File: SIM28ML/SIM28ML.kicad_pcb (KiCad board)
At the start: 2 copper layers, 22.7 x 20.3 mm, 26 parts, among them J1 Conn_01x05, J2 Conn_01x05, U2 AP7365-W-7

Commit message: GNSS Boards Page Layout Updates
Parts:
- renumbered SIM28M to SIM28ML
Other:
- board text added: "SIM28ML www.SirBoard.com"
- board text removed: "SIM28M www.SirBoard.com"
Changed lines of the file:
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@@
     (thickness 1.6)
     (drawings 26)
-    (tracks 116)
+    (tracks 117)
     (zones 0)
     (modules 26)
@@
   (page User 132.004 102.006)
   (title_block
-    (title "SIM28M Based GPS Module")
+    (title "SIM28ML Based GPS Module")
     (date 2019-10-30)
     (rev 1)
     (company SirBoard)
-    (comment 1 "SIM28M is based on the MT3339 Chipset")
+    (comment 1 "SIM28ML is based on the MT3339 Chipset")
     (comment 2 "Breadboard Friendly Micro GPS Module")
   )
@@
     (tags "Integrated Circuit")
     (attr smd)
-    (fp_text reference SIM28M (at 4.85 5.05 90) (layer F.SilkS)
+    (fp_text reference SIM28ML (at 4.85 5.05 90) (layer F.SilkS)
       (effects (font (size 1.27 1.27) (thickness 0.254)))
     )
@@
     )
   )
-  (gr_text "SIM28M\nwww.SirBoard.com" (at 63.5 31.242 180) (layer B.SilkS)
+  (gr_text "SIM28ML\nwww.SirBoard.com" (at 63.5 31.242 180) (layer B.SilkS)
     (effects (font (size 1 0.9) (thickness 0.15)) (justify mirror))
   )
@@
   (segment (start 58.3565 44.454419) (end 58.3565 45.6565) (width 0.6) (layer B.Cu) (net 23))
   (segment (start 58.3565 41.8365) (end 58.3565 44.454419) (width 0.6) (layer B.Cu) (net 23))
-  (segment (start 68.272 35.6235) (end 68.2625 35.633) (width 0.25) (layer F.Cu) (net 23))
-  (segment (start 69.596 35.6235) (end 68.272 35.6235) (width 0.25) (layer F.Cu) (net 23))
-  (segment (start 71.501 36.0045) (end 69.977 36.0045) (width 0.25) (layer F.Cu) (net 23))
-  (segment (start 69.977 36.0045) (end 69.596 35.6235) (width 0.25) (layer F.Cu) (net 23))
   (segment (start 58.3565 37.465) (end 58.3565 41.8365) (width 0.6) (layer B.Cu) (net 23))
   (segment (start 55.5365 36.7665) (end 57.658 36.7665) (width 0.6) (layer B.Cu) (net 23))
@@
   (segment (start 58.3565 41.8365) (end 66.812 41.8365) (width 0.6) (layer B.Cu) (net 23))
   (segment (start 66.812 41.8365) (end 68.326 40.3225) (width 0.6) (layer B.Cu) (net 23))
+  (segment (start 68.272 35.6235) (end 68.2625 35.633) (width 0.25) (layer F.Cu) (net 23))
+  (segment (start 69.596 35.6235) (end 68.272 35.6235) (width 0.25) (layer F.Cu) (net 23))
+  (segment (start 70.104 36.1315) (end 69.596 35.6235) (width 0.25) (layer F.Cu) (net 23))
+  (segment (start 71.501 36.0045) (end 71.374 36.1315) (width 0.25) (layer F.Cu) (net 23))
+  (segment (start 71.374 36.1315) (end 70.104 36.1315) (width 0.25) (layer F.Cu) (net 23))
   (segment (start 53.1495 37.3) (end 53.1875 37.338) (width 0.25) (layer F.Cu) (net 24))
   (via (at 52.6415 38.2905) (size 0.6) (drill 0.3) (layers F.Cu B.Cu) (net 24))

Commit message: Power LED added
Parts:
- removed R7: 68K, Resistor_SMD:R_0603_1608Metric
- removed R8: 22K, Resistor_SMD:R_0603_1608Metric
- removed U2: AP7365-W-7, Package_TO_SOT_SMD:SOT-23-5
- added 3V: LED, LED_SMD:LED_0603_1608Metric, F.Cu at (73.9, 39.0)
- added LED: SolderJumper_2_Bridged, Jumper:SolderJumper-2_P1.3mm_Bridged_RoundedPad1.0x1.5mm, B.Cu at (73.2, 33.3)
- added R6: 680E, Resistor_SMD:R_0603_1608Metric, F.Cu at (73.9, 36.1)
- added U1: AP2127K-3.3, Package_TO_SOT_SMD:SOT-23-5, F.Cu at (71.5, 36.1)
- moved ANT 0.95 mm to (53.8, 40.5)
- renumbered JP1 to ANT, CR1220 to BT1, SIM28ML to IC1
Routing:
- net Net-(R7-Pad2): track 2.96 -> 0.00 mm
- net EN: track 15.7 -> 13.3 mm
- net Net-(JP2-Pad2): track 0.00 -> 2.05 mm, vias 0 -> 1
- net Net-(D1-Pad2): track 0.00 -> 1.35 mm
- net 3V3: track 13.0 -> 12.1 mm, vias 2 -> 1

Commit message: Schematic PDF and 3D Renders added
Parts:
- renumbered BT1 to CR1220
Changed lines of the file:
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@@
   )
   (setup
-    (last_trace_width 0.4)
+    (last_trace_width 0.127)
     (user_trace_width 0.127)
     (user_trace_width 0.15)
@@
     (tags "Keystone type 3000 coin cell retainer")
     (attr smd)
-    (fp_text reference BT1 (at 0 3.937 180 unlocked) (layer B.SilkS)
+    (fp_text reference CR1220 (at 0 3.937 180 unlocked) (layer B.SilkS)
       (effects (font (size 1 1) (thickness 0.15)) (justify mirror))
     )

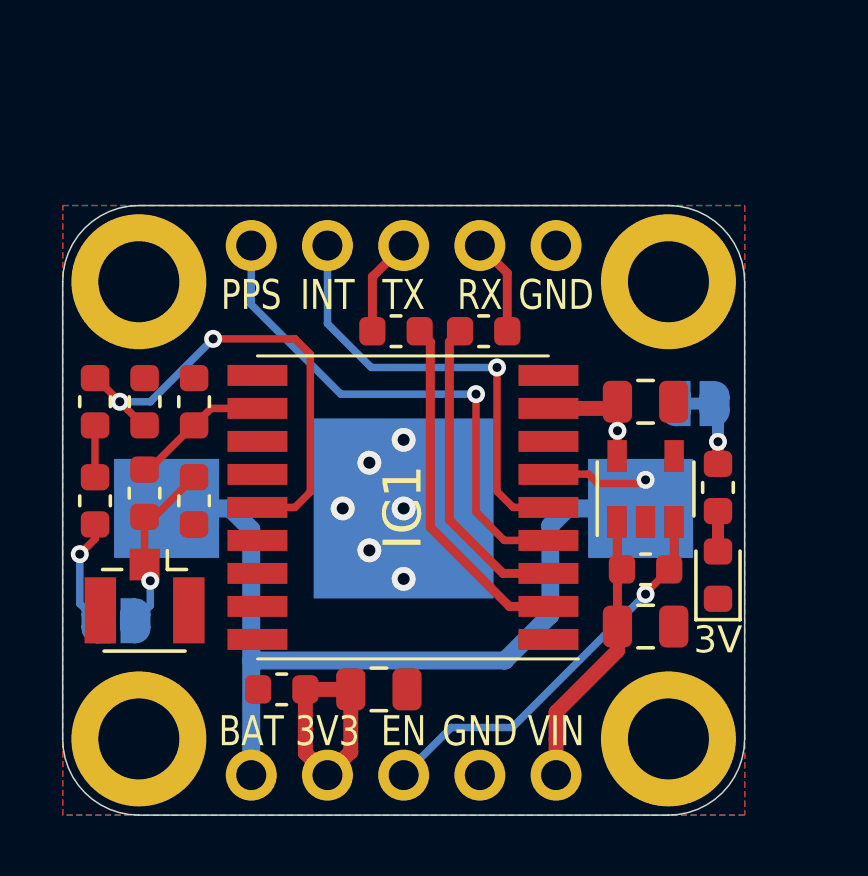
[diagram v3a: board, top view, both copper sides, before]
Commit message: Board Sizes Updated
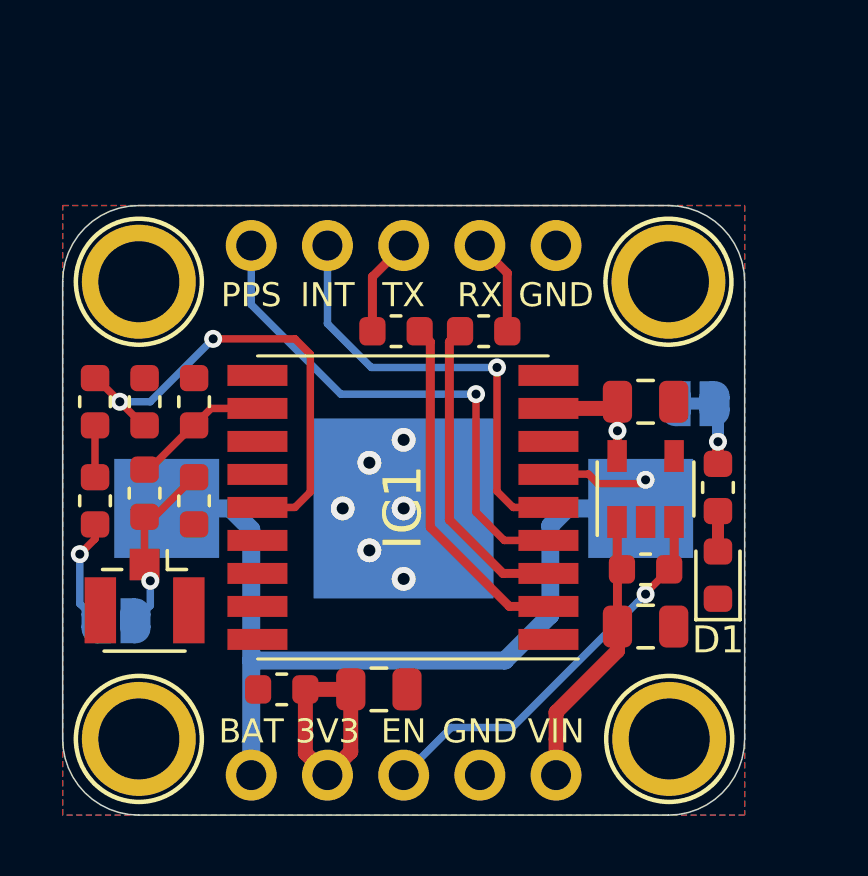
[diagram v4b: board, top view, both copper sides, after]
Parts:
- H1, H2, H3, H4: footprint MountingHole:MountingHole_2.7mm_M2.5_ISO14580_Pad -> SirBoardLibrary:MountingHole_M2.5_SirBoard
- moved H4 23.3 mm to (72.3, 44.5), turned to 0 degrees
- moved H2 23.3 mm to (54.6, 44.5), turned to 0 degrees
- moved H1 15.2 mm to (54.6, 29.2), turned to 0 degrees
- moved H3 15.2 mm to (72.3, 29.2), turned to 0 degrees
- renumbered CR1220 to BT1, 3V to D1, ANT to JP1, LED to JP2

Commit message: Soldermask width adjusted
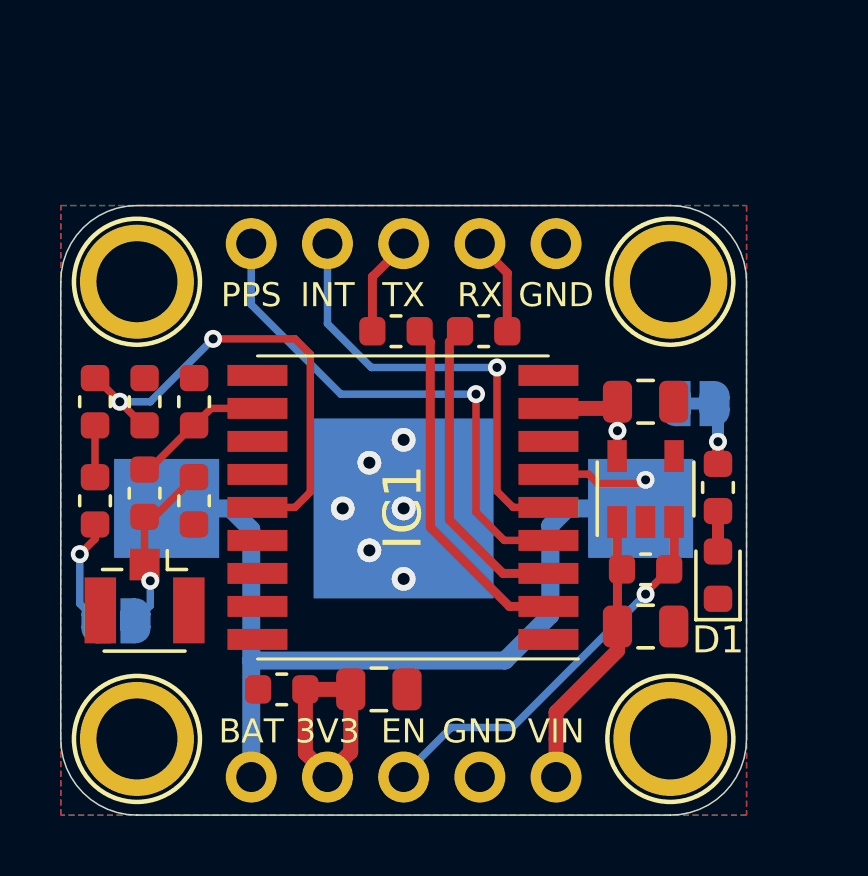
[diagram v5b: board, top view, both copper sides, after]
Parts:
- moved H1 0.06 mm to (54.5, 29.2)
- moved H2 0.06 mm to (54.5, 44.5)
- moved J1 0.06 mm to (68.5, 27.9)
- moved J2 0.06 mm to (68.5, 45.7)
- moved H3 0.06 mm to (72.3, 29.2)
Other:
- board size 22.7 x 20.3 mm -> 22.9 x 20.3 mm
- rule solder_mask_min_width: 0.1 -> 0.05

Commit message: SIM28ML Revision2
Active Antenna components removed, Battery connector changed
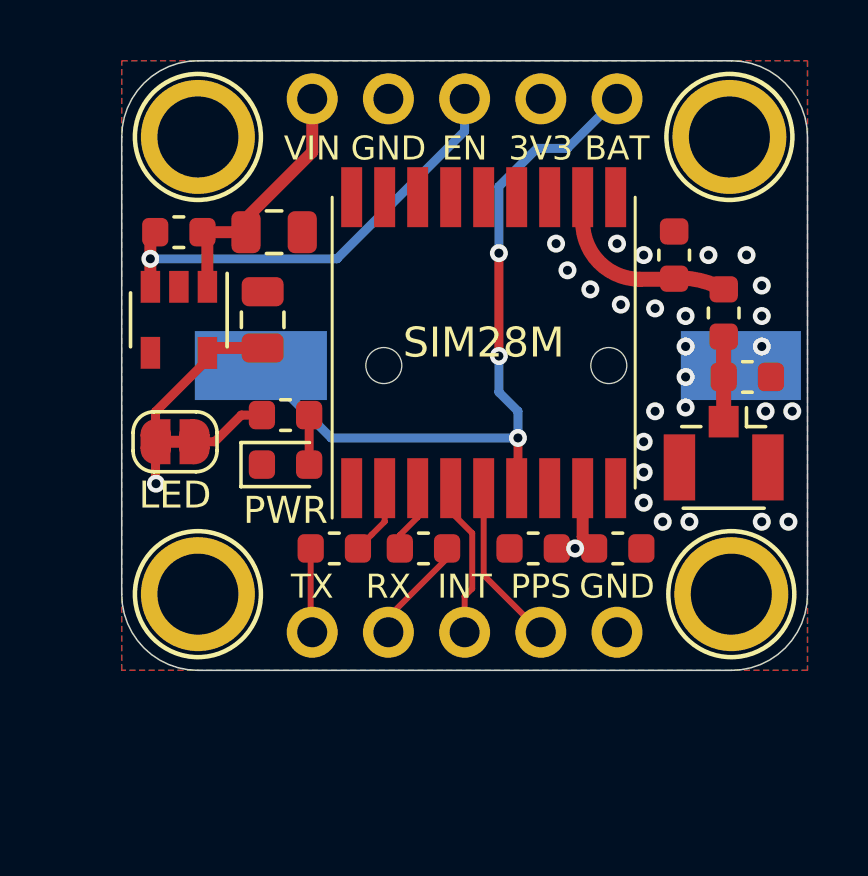
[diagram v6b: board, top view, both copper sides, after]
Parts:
- removed C6: 100nF, Capacitor_SMD:C_0603_1608Metric
- removed D1: LED, LED_SMD:LED_0603_1608Metric
- removed JP1: SolderJumper_2_Open, Jumper:SolderJumper-2_P1.3mm_Open_RoundedPad1.0x1.5mm
- removed L1: 27n, Inductor_SMD:L_0603_1608Metric
- removed R5: 10R, Resistor_SMD:R_0603_1608Metric
- added G***: LOGO, logo:SirBoard127x40, B.Cu at (66.5, 32.0)
- added G***: LOGO, logo:OSHW36x26, B.Cu at (56.8, 28.7)
- added G***: LOGO, logo:logo29x41, B.Cu at (57.0, 35.8)
- added PWR: LED, LED_SMD:LED_0603_1608Metric, F.Cu at (59.5, 35.3)
- BT1: footprint Battery:BatteryHolder_Keystone_3000_1x12mm -> SirBoardLibrary:S8411-45R_1
- C1: value 4u7 -> 4.7uF; footprint Capacitor_SMD:C_0805_2012Metric -> Capacitor_SMD:C_0603_1608Metric
- C3, C4: value 1uF -> 10uF
- JP2: moved to F.Cu
- moved J2 24.0 mm to (60.4, 23.1), turned to 270 degrees
- moved H1 22.4 mm to (74.4, 39.6), turned to 180 degrees
- moved R4 20.2 mm to (74.1, 30.3)
- moved H2 20.2 mm to (56.6, 24.4), turned to 180 degrees
- moved AE1 19.9 mm to (74.1, 34.9)
- moved R3 19.2 mm to (55.9, 27.6), turned to 180 degrees
- moved C7 18.9 mm to (74.9, 32.4), turned to 0 degrees
- moved C3 18.1 mm to (59.1, 27.6)
- moved JP2 17.4 mm to (55.8, 34.5)
- moved C5 16.7 mm to (72.5, 28.3)
- moved U1 16.5 mm to (55.9, 30.5), turned to 270 degrees
- moved H4 16.5 mm to (56.6, 39.6), turned to 180 degrees
- moved J1 15.3 mm to (60.4, 40.9), turned to 270 degrees
- moved R6 14.6 mm to (59.5, 33.7), turned to 180 degrees
- moved C4 13.1 mm to (58.7, 30.5), turned to 90 degrees
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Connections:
- net Net-(C5-Pad1) renamed /ANT
- J1 pad 1: GND -> TXD0
- J1 pad 3: TXD0 -> PPS
- J1 pad 5: PPS -> GND
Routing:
- net Net-(IC1-Pad14): track 16.3 -> 0.00 mm, vias 2 -> 0
- net PPS: track 17.4 -> 5.21 mm, vias 1 -> 0
- net Net-(IC1-Pad2): track 11.7 -> 2.38 mm
- net INT: track 14.9 -> 5.59 mm, vias 1 -> 0
- net Net-(IC1-Pad3): track 10.5 -> 2.26 mm
- net VBAT: track 31.4 -> 25.1 mm, vias 1 -> 3
- net /ANT: track 4.90 -> 0.00 mm
- net Net-(JP1-Pad1): track 3.71 -> 0.00 mm, vias 1 -> 0
- net Net-(AE1-Pad1): track 5.95 -> 2.84 mm, vias 1 -> 0
- net EN: track 13.3 -> 15.2 mm
- net Net-(L1-Pad2): track 1.73 -> 0.00 mm
- net 3V3: track 12.1 -> 10.4 mm, vias 1 -> 2
- net VIN: track 9.40 -> 8.70 mm
- net Net-(JP2-Pad2): track 2.05 -> 2.61 mm, vias 1 -> 0
- net GND: vias 6 -> 26
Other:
- board text added: "CR1220"
- board text added: "LED"
- board text added: "www.SirBoard.com"
- board text removed: "SIM28ML www.SirBoard.com"
